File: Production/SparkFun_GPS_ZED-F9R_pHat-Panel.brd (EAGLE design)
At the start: 144.2 x 142.7 mm, 454 parts, among them J1 U.FL, J10 QWIIC_RIGHT_ANGLE, J13 U.FL, J15 RASPBERRYPI-40-PIN-GPIO_SMD_S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, J16 QWIIC_RIGHT_ANGLE, J19 U.FL, J21 RASPBERRYPI-40-PIN-GPIO_SMD_S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, J22 QWIIC_RIGHT_ANGLE, J5 QWIIC_RIGHT_ANGLE, J6 RASPBERRYPI-40-PIN-GPIO_SMD_S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

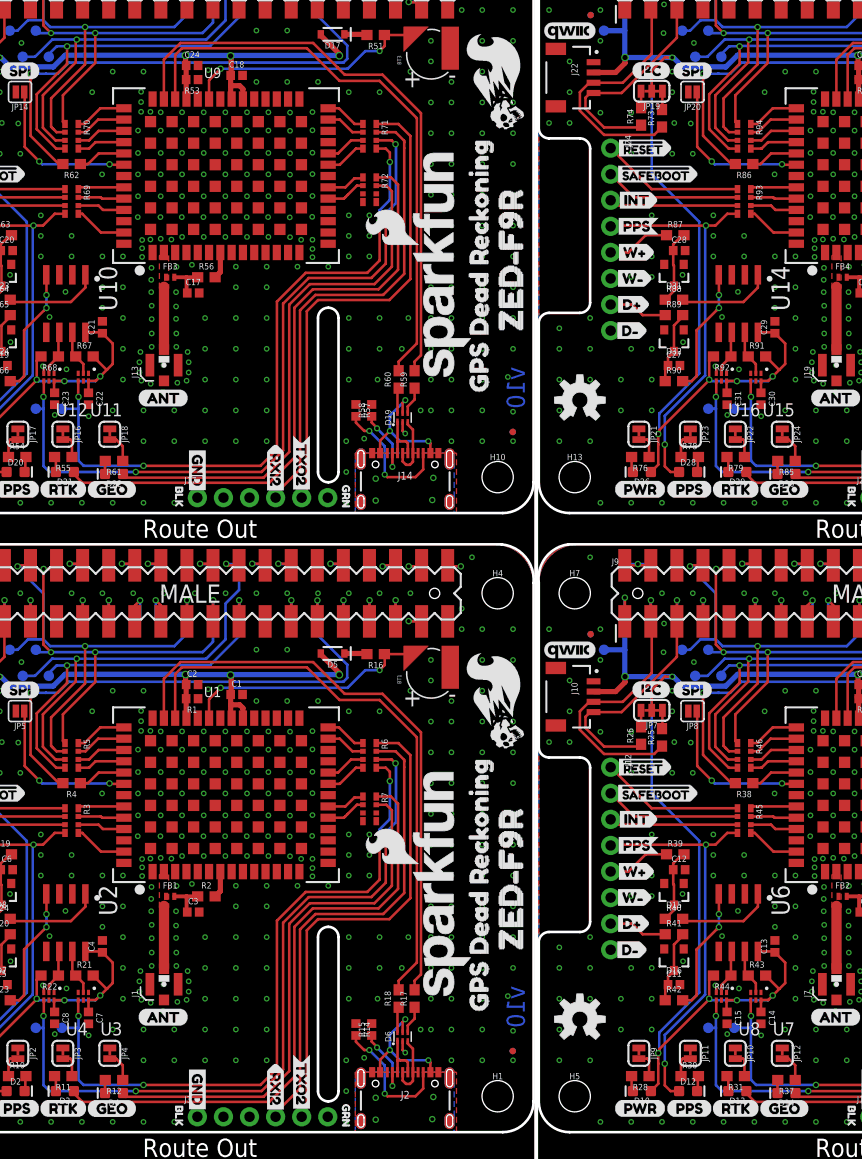
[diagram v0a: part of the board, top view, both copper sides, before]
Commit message: Fixes issue with panel
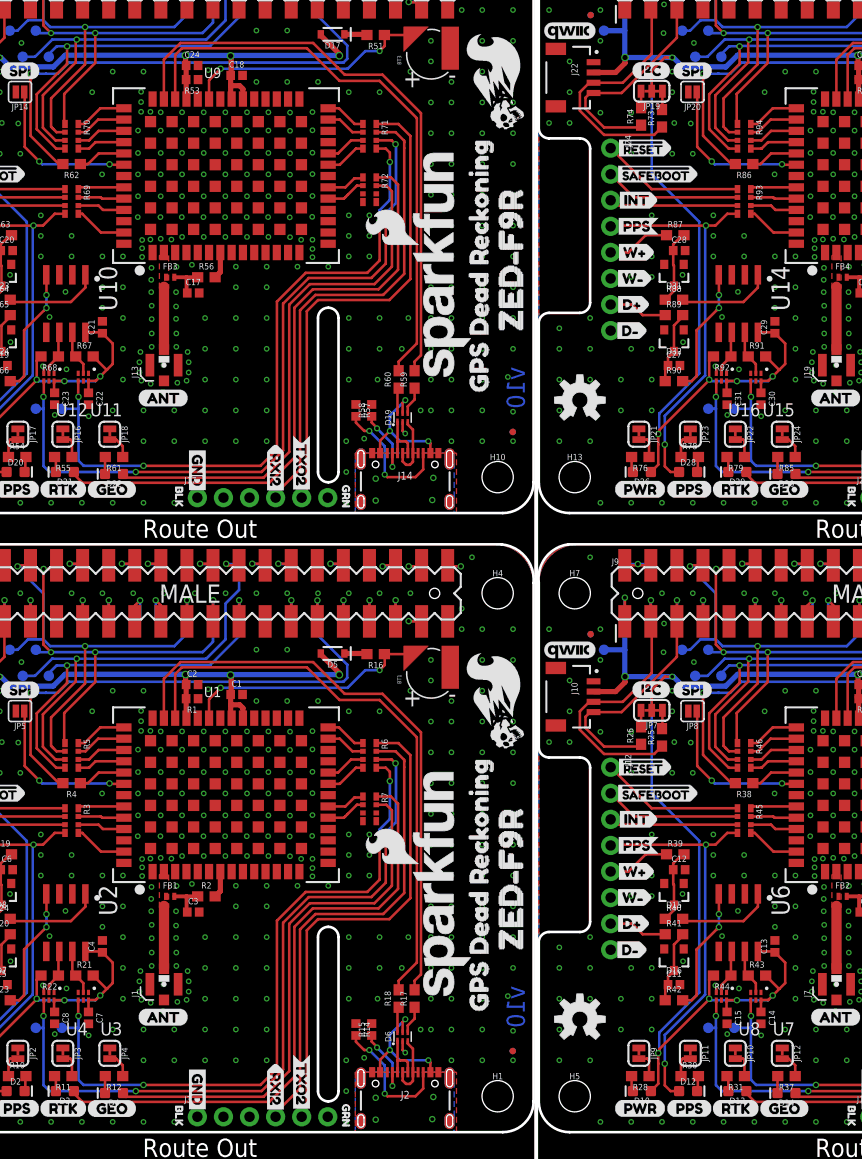
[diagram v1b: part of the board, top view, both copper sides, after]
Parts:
- moved R12 0.38 mm to (24.1, 5.46)
- moved R37 0.38 mm to (89.6, 5.46)
- moved R61 0.38 mm to (24.1, 65.8)
- moved R85 0.38 mm to (89.6, 65.8)
